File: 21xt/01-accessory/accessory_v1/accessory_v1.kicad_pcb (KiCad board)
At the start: 4 copper layers, 96.5 x 79 mm, 81 parts, among them IC1 LT6658AHMSE-2.5#PBF, IC2 LT6658AHMSE-5#PBF, IC3 REF5025AIDR, IC4 INA821IDGKT, IC5 INA821IDGKT, IC6 TXB0108PWR, IC7 REF5050IDR, IC8 INA821IDGKT, IC9 AD7175-8BCPZ-RL7, J1 Conn_01x04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

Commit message: Added all accessory Rev1 3d models, added 3d models to 3d model folder and updated footprints
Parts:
- removed C16: 1u, Capacitor_SMD:C_0603_1608Metric
- removed D4, D5: D_Schottky, Diode_SMD:D_0603_1608Metric
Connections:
- net 2.5v renamed 2v5
- net 3V3 renamed 3v3
- C1 pad 1: usb_gnd -> GNDA
- C10 pad 2: usb_gnd -> GNDA
- C11 pad 1: 2.5v_ref -> 2v5_ref
- C11 pad 2: usb_gnd -> GNDA
- C12 pad 2: usb_gnd -> GNDA
- C13 pad 2: usb_gnd -> GNDA
- C14 pad 2: usb_gnd -> GNDA
- C15 pad 2: usb_gnd -> GNDA
- C17 pad 1: 5v_ref -> 5v_reful
- C17 pad 2: usb_gnd -> GNDA
- C18 pad 2: usb_gnd -> GNDA
- C19 pad 2: usb_gnd -> GNDA
- C2 pad 1: usb_gnd -> GNDA
- C20 pad 2: usb_gnd -> GNDA
- C21 pad 2: usb_gnd -> GNDA
- C22 pad 1: usb_gnd -> GNDA
- C23 pad 1: usb_gnd -> GNDA
- C24 pad 2: usb_gnd -> GNDA
- C25 pad 2: usb_gnd -> GNDA
- C26 pad 2: usb_gnd -> GNDA
- C27 pad 2: usb_gnd -> GNDA
- C3 pad 1: usb_gnd -> GNDA
- C31 pad 2: usb_gnd -> GNDA
- C32 pad 2: usb_gnd -> GNDA
- C33 pad 1: usb_gnd -> GNDA
- C34 pad 1: usb_gnd -> GNDA
- C35 pad 2: usb_gnd -> GNDA
- C36 pad 2: usb_gnd -> GNDA
- C37 pad 2: usb_gnd -> GNDA
- C38 pad 2: usb_gnd -> GNDA
- C39 pad 2: usb_gnd -> GNDA
- C4 pad 1: usb_gnd -> GNDA
- C40 pad 2: usb_gnd -> GNDA
- C5 pad 1: usb_gnd -> GNDA
- C6 pad 1: usb_gnd -> GNDA
- C7 pad 1: usb_gnd -> GNDA
- C8 pad 1: usb_gnd -> GNDA
- C9 pad 2: usb_gnd -> GNDA
- IC1 pad 1: usb_gnd -> GNDA
- IC1 pad 17: usb_gnd -> GND1
- IC1 pad 2: usb_gnd -> GNDA
- IC1 pad 6: usb_gnd -> GNDA
- IC2 pad 1: usb_gnd -> GNDA
- IC2 pad 17: usb_gnd -> GNDA
- IC2 pad 2: usb_gnd -> GNDA
- IC2 pad 6: usb_gnd -> GNDA
- IC3 pad 4: usb_gnd -> GNDA
- IC3 pad 5: unconnected-(IC3-TRIM/NR-Pad5) -> Net-(IC3-TRIM/NR)
- IC3 pad 6: Net-(D4-A) -> 2v5_ref
- IC4 pad 6: 2.5v_ref -> 2v5_ref
- IC5 pad 6: 2.5v_ref -> 2v5_ref
- IC6 pad 11: usb_gnd -> GNDA
- IC6 pad 19: 5v_ref -> 5v_reful
- IC7 pad 4: usb_gnd -> GNDA
- IC7 pad 5: unconnected-(IC7-TRIM/NR-Pad5) -> Net-(IC7-TRIM/NR)
- IC7 pad 6: Net-(D5-A) -> 5v_ref
- IC8 pad 6: 2.5v_ref -> 2v5_ref
- IC9 pad 11: usb_gnd -> GNDA
- IC9 pad 19: usb_gnd -> GNDA
- IC9 pad 21: usb_gnd -> GNDA
- IC9 pad 28: brakespeed2 -> brakepressure2
- IC9 pad 29: brakespeed1 -> brakepressure1
- IC9 pad 39: usb_gnd -> GNDA
- IC9 pad 41: usb_gnd -> GNDA
- IC9 pad 8: usb_gnd -> GNDA
- J1 pad 1: usb_gnd -> GNDA
- J1 pad 2: usb_gnd -> GNDA
- J2 pad 10: usb_gnd -> GNDA
- J2 pad 11: usb_gnd -> GNDA
- J2 pad 15: usb_gnd -> GNDA
- J2 pad 25: brakespeed1 -> brakepressure1
- J2 pad 26: usb_gnd -> GNDA
- J2 pad 27: usb_gnd -> GNDA
- J2 pad 28: usb_gnd -> GNDA
- J2 pad 29: usb_gnd -> GNDA
- J2 pad 30: usb_gnd -> GNDA
- J2 pad 7: brakespeed2 -> brakepressure2
- J2 pad 9: usb_gnd -> GNDA
- J2 pad MH1: usb_gnd -> GNDA
- J2 pad MH2: usb_gnd -> GNDA
- J3 pad 2: usb_gnd -> GNDA
- J6 pad 1: usb_gnd -> GNDA
- PS1 pad 1: usb_gnd -> GNDA
- PS1 pad 5: usb_gnd -> GNDA
- R10 pad 2: usb_gnd -> GNDA
- R8 pad 2: usb_gnd -> GNDA
- R9 pad 2: usb_gnd -> GNDA
- TP3 pad 1: 2.5v_ref -> 2v5_ref
- U1 pad GND1: usb_gnd -> GNDA
- U1 pad GND2: usb_gnd -> GNDA
- U1 pad GND3: usb_gnd -> GNDA
- U1 pad GND4: usb_gnd -> GNDA
- U1 pad GND5: usb_gnd -> GNDA
- U1 pad USB_GND1: usb_gnd -> GNDA
- U1 pad USB_GND2: usb_gnd -> GNDA
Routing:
- net usb_gnd: track 190.0 -> 12.1 mm, vias 16 -> 1
- net GNDA: track 0.00 -> 177.9 mm, vias 0 -> 15
- net 2v5_ref: track 0.00 -> 59.5 mm, vias 0 -> 6
- net 2.5v_ref: track 55.3 -> 0.00 mm, vias 6 -> 0
- net Net-(D4-A): track 4.25 -> 0.00 mm
- net Net-(D5-A): track 3.84 -> 0.00 mm
- net 5v_ref: track 52.5 -> 56.3 mm

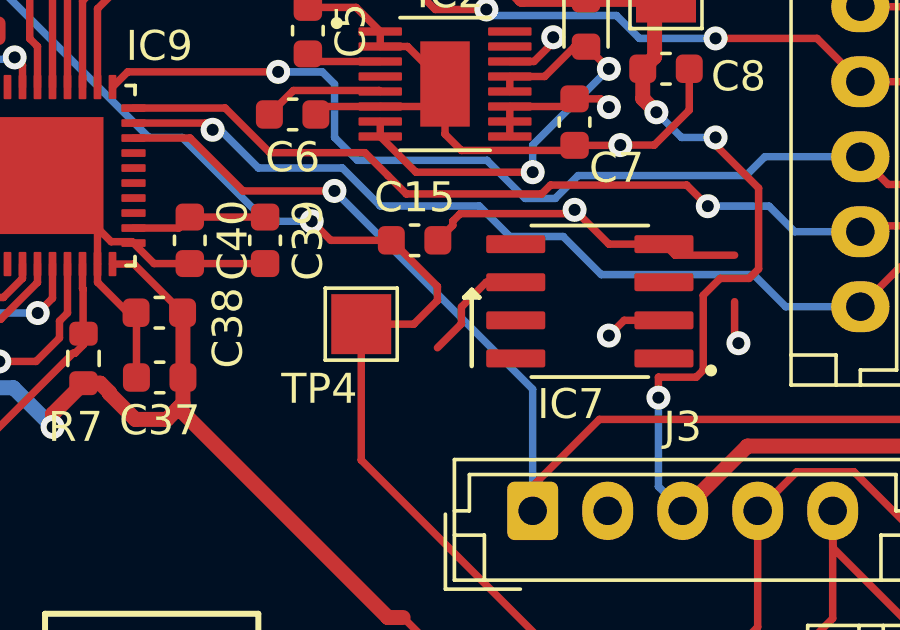
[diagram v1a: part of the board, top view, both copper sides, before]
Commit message: Accessory V2 schematic almost done, only missing TVS diodes and checking
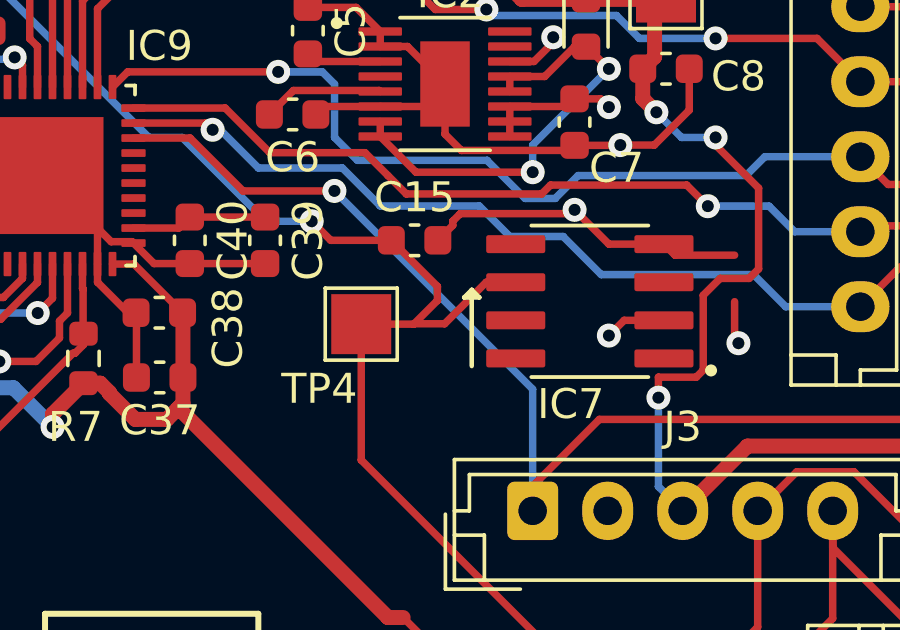
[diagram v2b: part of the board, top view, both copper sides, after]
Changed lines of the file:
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@@
   (segment (start 106.299 47.535) (end 106.299 50.499) (width 0.25) (layer "B.Cu") (net 10))
   (segment (start 106.230847 38.022542) (end 107.070305 38.862) (width 0.25) (layer "B.Cu") (net 10))
-  (segment (start 99.733 44.513001) (end 99.733 45.0725) (width 0.25) (layer "F.Cu") (net 11))
   (segment (start 82.537 36.117) (end 82.537 33.655) (width 0.25) (layer "F.Cu") (net 11))
-  (segment (start 99.733 45.0725) (end 98.933 45.8725) (width 0.25) (layer "F.Cu") (net 11))
   (segment (start 96.393 49.614999) (end 105.717001 58.939) (width 0.25) (layer "F.Cu") (net 11))
   (segment (start 83.602 37.182) (end 82.537 36.117) (width 0.25) (layer "F.Cu") (net 11))
@@
   (segment (start 97.396 42.291) (end 95.377 42.291) (width 0.25) (layer "F.Cu") (net 11))
   (segment (start 97.396 42.291) (end 98.933 43.828) (width 0.25) (layer "F.Cu") (net 11))
+  (segment (start 99.173501 45.0725) (end 98.158 45.0725) (width 0.25) (layer "F.Cu") (net 11))
   (segment (start 101.543 43.688) (end 100.558001 43.688) (width 0.25) (layer "F.Cu") (net 11))
   (segment (start 98.933 43.828) (end 98.933 44.2975) (width 0.25) (layer "F.Cu") (net 11))
   (segment (start 105.717001 58.939) (end 106.502 58.939) (width 0.25) (layer "F.Cu") (net 11))
+  (segment (start 100.558001 43.688) (end 99.173501 45.0725) (width 0.25) (layer "F.Cu") (net 11))
   (segment (start 107.974 58.939) (end 106.502 58.939) (width 0.25) (layer "F.Cu") (net 11))
+  (segment (start 98.158 45.0725) (end 98.1455 45.085) (width 0.25) (layer "F.Cu") (net 11))
   (segment (start 96.393 45.085) (end 98.1455 45.085) (width 0.25) (layer "F.Cu") (net 11))
   (segment (start 98.1455 45.085) (end 98.933 44.2975) (width 0.25) (layer "F.Cu") (net 11))
   (segment (start 95.377 42.291) (end 94.742 41.656) (width 0.25) (layer "F.Cu") (net 11))
-  (segment (start 100.558001 43.688) (end 99.733 44.513001) (width 0.25) (layer "F.Cu") (net 11))
   (segment (start 96.393 45.085) (end 96.393 49.614999) (width 0.25) (layer "F.Cu") (net 11))
   (via (at 81.788 32.512) (size 0.8) (drill 0.4) (layers "F.Cu" "B.Cu") (net 11))
